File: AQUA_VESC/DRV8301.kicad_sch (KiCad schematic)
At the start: 62 parts, among them U6 TP2604-SR, U7 DRV8301QDCAQ1, U8 22uH, U9 AMS1117-3.3

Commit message: AQUA VESC仮完成
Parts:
- C30: value 15n -> 10n
- U6: renamed from U7; footprint specific_footprint_library:DCA56_6P35X3P61 -> specific_footprint_library:HTSSOP-56_L14.0-W6.0-P0.50-LS8.0-BL
- renumbered R15 to R14, R16 to R15, R17 to R16, R18 to R17, R19 to R18, R20 to R19, R21 to R20, R22 to R21, R23 to R22, R24 to R23, R25 to R24, R26 to R25, R27 to R26, R28 to R27, R29 to R28, R30 to R29, R31 to R30, R32 to R31, R33 to R32, R34 to R33, R35 to R34, R36 to R35, R37 to R36, R38 to R37, U6 to U5, U8 to U7, U9 to U8
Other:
- note added: "0.1u, ≥16V"
- note added: "22n, @Vpvdd"
- note added: ">1u"
- note added: "fsw = 500kHz"
- note added: "tss = Css*Vref*0.8/Iss = 10nF*0.8V*0.8/2uA = 3.2ms"

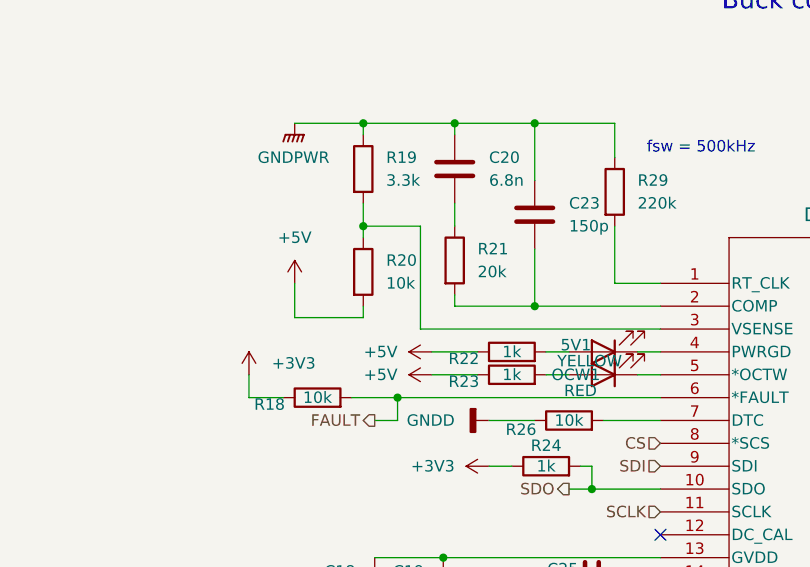
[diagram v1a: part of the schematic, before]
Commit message: AQUA_VESC REV01作成
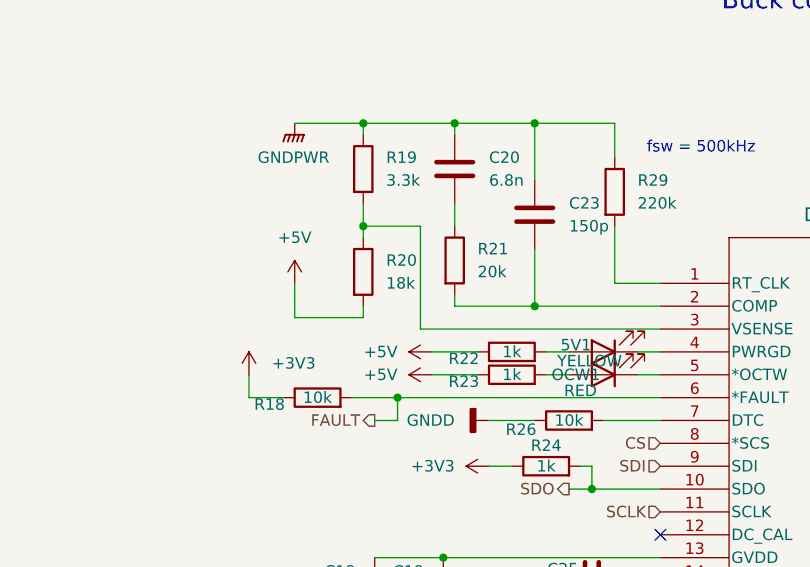
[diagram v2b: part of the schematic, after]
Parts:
- R20: value 10k -> 18k
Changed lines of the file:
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@@
 			)
 		)
-		(property "Value" "10k"
+		(property "Value" "18k"
 			(at 64.77 62.2299 0)
 			(effects

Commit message: 制御基板REV01完成
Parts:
- renumbered R14 to R13, R15 to R14, R16 to R15, R17 to R16, R18 to R17, R19 to R18, R20 to R19, R21 to R20, R22 to R21, R23 to R22, R24 to R23, R25 to R24, R26 to R25, R27 to R26, R28 to R27, R29 to R28, R30 to R29, R31 to R30, R32 to R31, R33 to R32, R34 to R33, R35 to R34, R36 to R35, R37 to R36

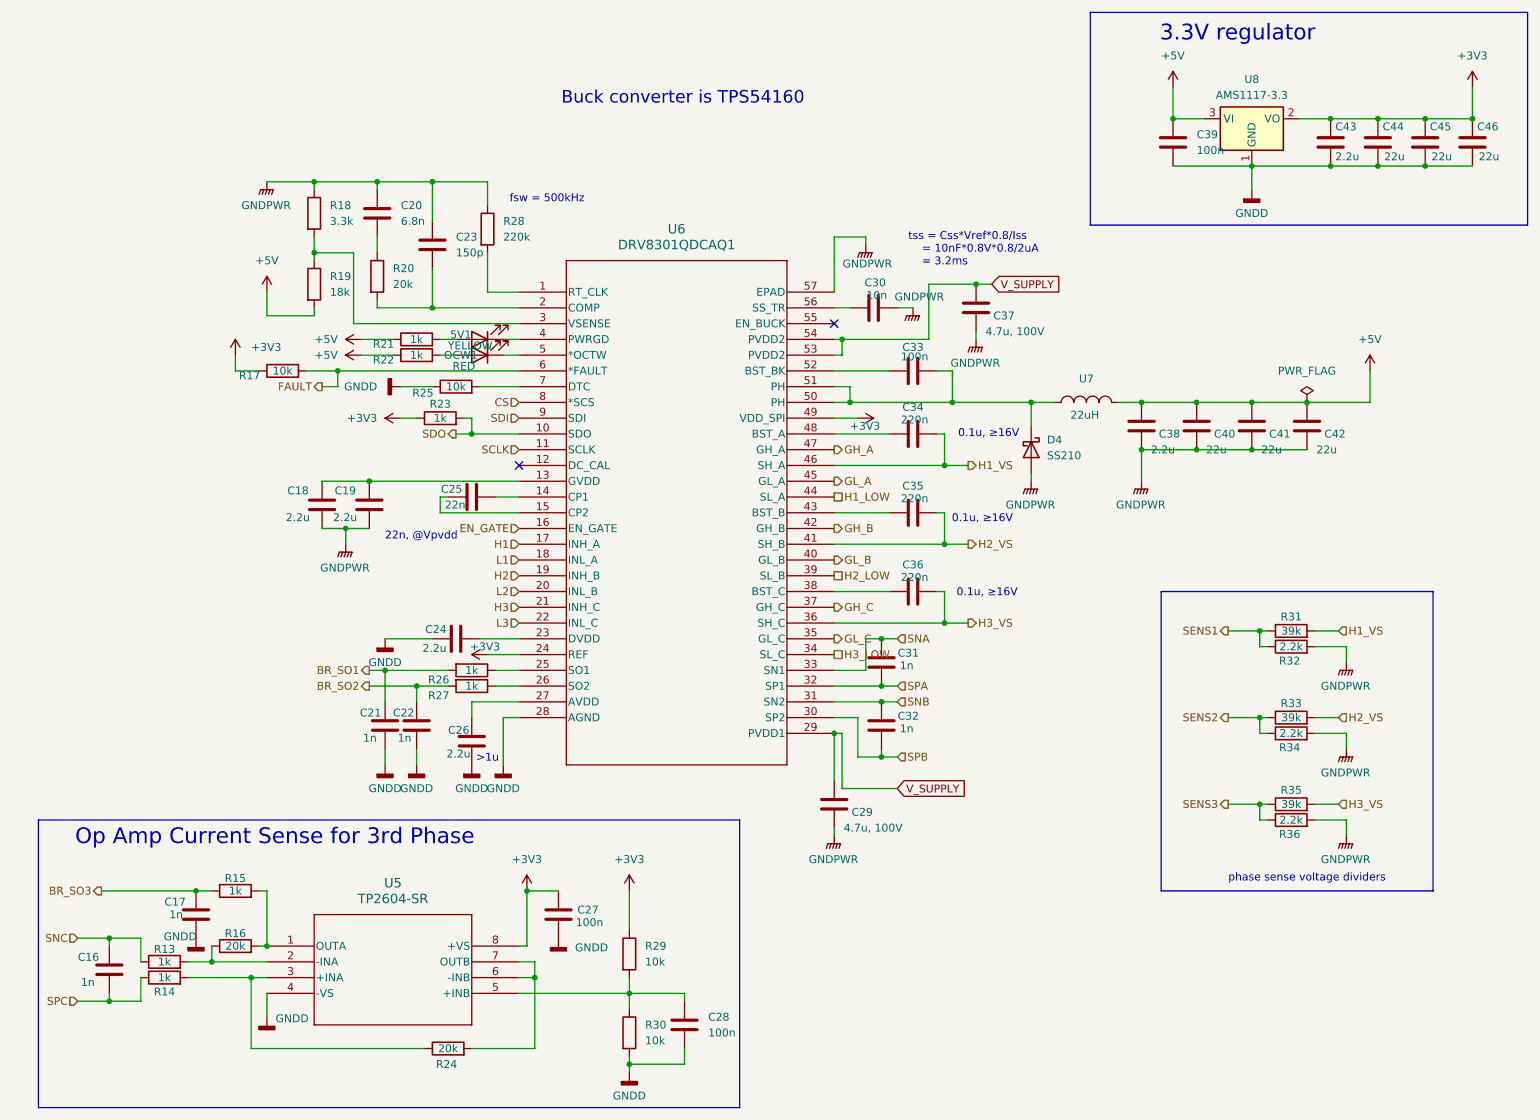
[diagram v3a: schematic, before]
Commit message: 方針変更、back_connector_escにMT60を使用しないことに
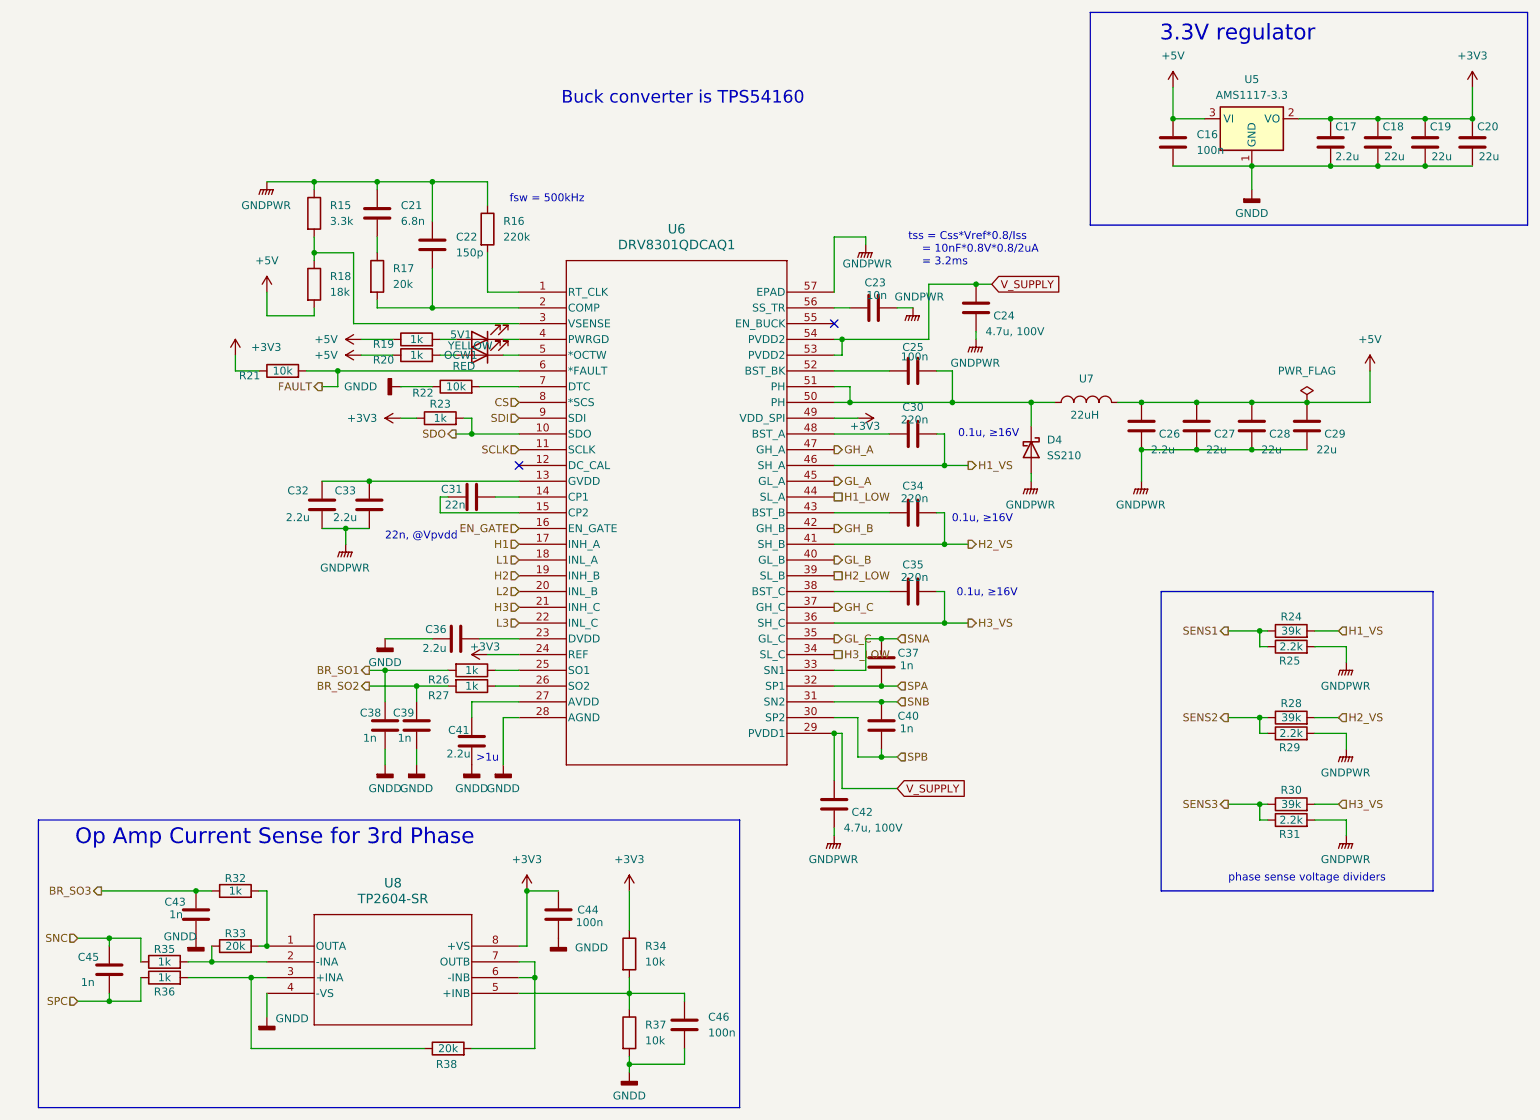
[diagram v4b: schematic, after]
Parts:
- renumbered C39 to C16, C43 to C17, C44 to C18, C45 to C19, C46 to C20, C20 to C21, C23 to C22, C30 to C23, C37 to C24, C33 to C25, C38 to C26, C40 to C27, C41 to C28, C42 to C29, C34 to C30, C25 to C31, C18 to C32, C19 to C33, C35 to C34, C36 to C35, C24 to C36, C31 to C37, C21 to C38, C22 to C39, C32 to C40, C26 to C41, C29 to C42, C17 to C43, C27 to C44, C16 to C45, C28 to C46, R18 to R15, R28 to R16, R20 to R17, R19 to R18, R21 to R19, R22 to R20, R17 to R21, R25 to R22, R31 to R24, R32 to R25, R33 to R28, R34 to R29, R35 to R30, R36 to R31, R15 to R32, R16 to R33, R29 to R34, R13 to R35, R14 to R36, R30 to R37, R24 to R38, U8 to U5, U5 to U8
